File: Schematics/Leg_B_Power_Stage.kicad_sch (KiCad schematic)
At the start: 38 parts, among them Q4 C3M0025065K, Q5 C3M0025065K, U3 UCC21710QDWRQ1, U4 UCC21710QDWRQ1

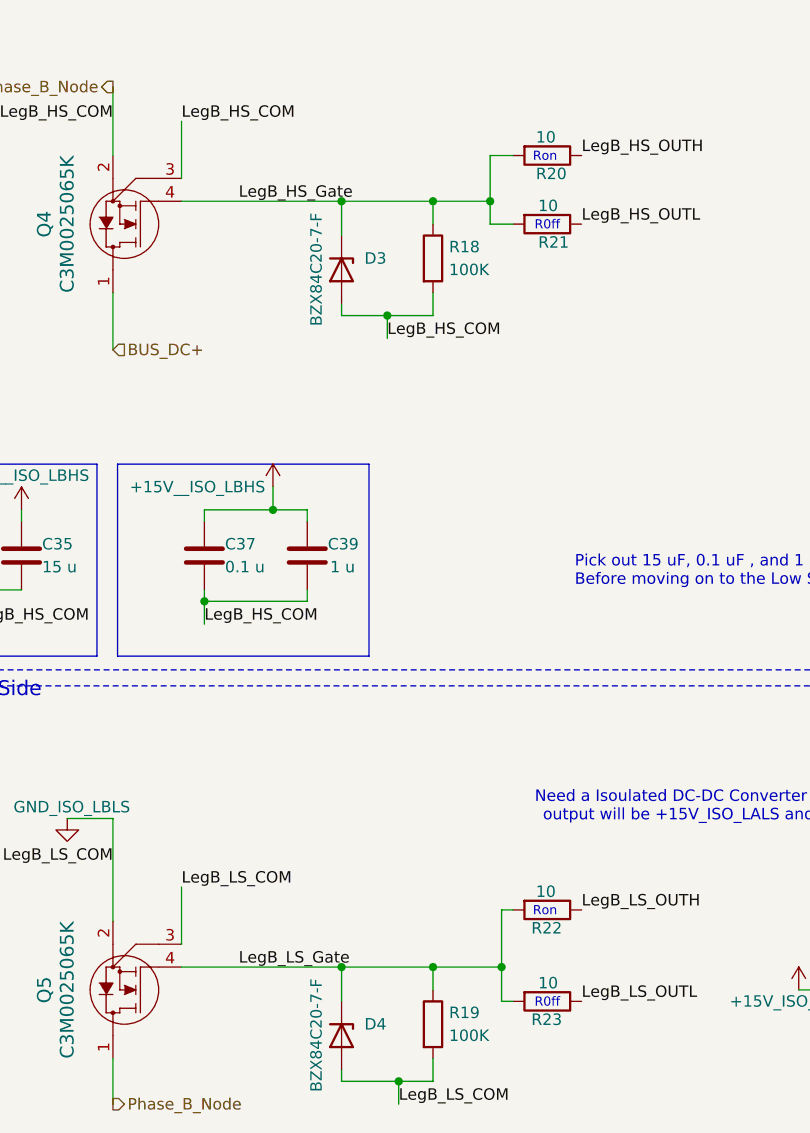
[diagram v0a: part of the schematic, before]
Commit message: [Milestone Compelted Controller and USB]
- Added Test Points
- Completed USB circuit to Controller
- Wired up Controller
- Added Connectors to Power Subsheet and 12pin from cotnroller to Full
  Bridge
- Added 3d models for USB compoents
- General fixes to subsheets
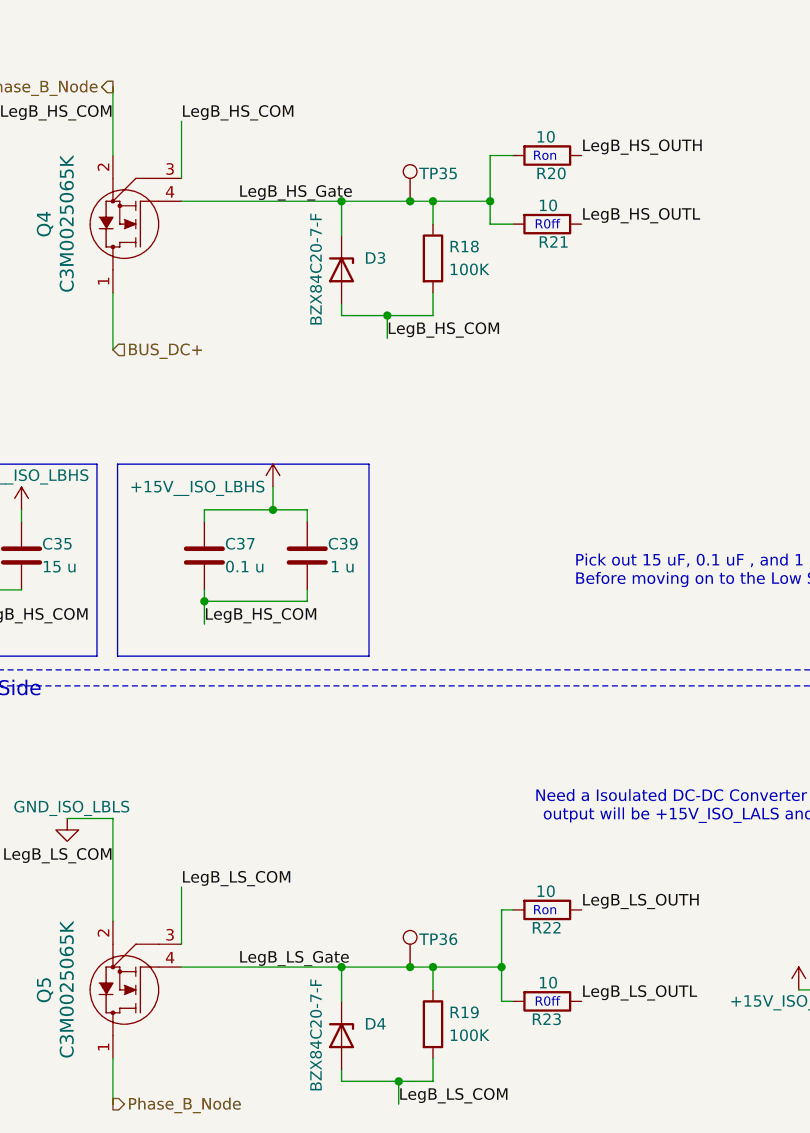
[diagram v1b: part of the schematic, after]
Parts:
- added TP35, TP36: 5277, SiC_Inverter:5277, symbol SiC_Inverter:5277
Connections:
- net LegB_HS_Gate: now also TP35.1
- net LegB_LS_Gate: now also TP36.1
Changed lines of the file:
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@@
 	)
 	(junction
+		(at 67.31 54.61)
+		(diameter 0)
+		(color 0 0 0 0)
+	)
+	(junction
 		(at 181.61 69.85)
 		(diameter 0)
@@
 	)
 	(junction
+		(at 67.31 139.7)
+		(diameter 0)
+		(color 0 0 0 0)
+	)
+	(junction
 		(at 207.01 53.34)
 		(diameter 0)
@@
 	(wire
 		(pts
-			(xy 59.69 54.61) (xy 69.85 54.61)
+			(xy 59.69 54.61) (xy 67.31 54.61)
 		)
 		(stroke
@@
 	(wire
 		(pts
-			(xy 59.69 139.7) (xy 69.85 139.7)
+			(xy 59.69 139.7) (xy 67.31 139.7)
 		)
 		(stroke
@@
 	(wire
 		(pts
+			(xy 67.31 54.61) (xy 69.85 54.61)
+		)
+		(stroke
+			(width 0)
+			(type default)
+		)
+	)
+	(wire
+		(pts
 			(xy 69.85 139.7) (xy 69.85 142.24)
 		)
@@
 	(wire
 		(pts
+			(xy 67.31 139.7) (xy 69.85 139.7)
+		)
+		(stroke
+			(width 0)
+			(type default)
+		)
+	)
+	(wire
+		(pts
 			(xy 44.45 88.9) (xy 44.45 90.17)
 		)
@@
 	)
 	(symbol
+		(lib_id "SiC_Inverter:5277")
+		(at 67.31 139.7 0)
+		(unit 1)
+		(exclude_from_sim no)
+		(in_bom yes)
+		(on_board yes)
+		(dnp no)
+		(property "Reference" "TP36"
+			(at 68.326 136.652 0)
+			(effects
+				(font
+					(size 1.27 1.27)
+				)
+				(justify left)
+			)
+		)
+		(property "Value" "5277"
+			(at 51.308 152.654 0)
+			(effects
+				(font
+					(size 1.27 1.27)
+				)
+				(hide yes)
+			)
+		)
+		(property "Footprint" "SiC_Inverter:5277"
+			(at 57.404 150.876 0)
+			(effects
+				(font
+					(size 1.27 1.27)
+				)
+				(hide yes)
+			)
+		)
+		(property "Datasheet" "https://www.keyelco.com/userAssets/file/K75p62.pdf"
+			(at 75.184 147.066 0)
+			(effects
+				(font
+					(size 1.27 1.27)
+				)
+				(hide yes)
+			)
+		)
+		(property "Description" "Test Plugs & Test Jacks TEST POINT (BLUE) - COMPACT"
+			(at 77.724 149.098 0)
+			(effects
+				(font
+					(size 1.27 1.27)
+				)
+				(hide yes)
+			)
+		)
+		(pin "1"
+		)
+		(instances
+			(project "SiC_Single_Phase_Inverter"
+				(path "/a1ed0539-9735-4ad1-a8fd-87e26e7fce16/b6e78e1f-718a-4f31-892b-d9c389541b0d/d1761b4e-8a42-4386-8dfd-35f782fbcef3"
+					(reference "TP36")
+					(unit 1)
+				)
+			)
+		)
+	)
+	(symbol
 		(lib_id "SiC_Inverter:C3216X5R1E156M160AB")
 		(at 24.13 93.98 0)
@@
 					(unit 1)
 				)
+			)
+		)
+	)
+	(symbol
+		(lib_id "SiC_Inverter:5277")
+		(at 67.31 54.61 0)
+		(unit 1)
+		(exclude_from_sim no)
+		(in_bom yes)
+		(on_board yes)
+		(dnp no)
+		(property "Reference" "TP35"
+			(at 68.326 51.562 0)
+			(effects
+				(font
+					(size 1.27 1.27)
+				)
+				(justify left)
+			)
+		)
+		(property "Value" "5277"
+			(at 51.308 67.564 0)
+			(effects
+				(font
+					(size 1.27 1.27)
+				)
+				(hide yes)
+			)
+		)
+		(property "Footprint" "SiC_Inverter:5277"
+			(at 57.404 65.786 0)
+			(effects
+				(font
+					(size 1.27 1.27)
+				)
+				(hide yes)
+			)
+		)
+		(property "Datasheet" "https://www.keyelco.com/userAssets/file/K75p62.pdf"
+			(at 75.184 61.976 0)
+			(effects
+				(font
+					(size 1.27 1.27)
+				)
+				(hide yes)
+			)
+		)
+		(property "Description" "Test Plugs & Test Jacks TEST POINT (BLUE) - COMPACT"
+			(at 77.724 64.008 0)
+			(effects
+				(font
+					(size 1.27 1.27)
+				)
+				(hide yes)
+			)
+		)
+		(pin "1"
+		)
+		(instances
+			(project "SiC_Single_Phase_Inverter"
+				(path "/a1ed0539-9735-4ad1-a8fd-87e26e7fce16/b6e78e1f-718a-4f31-892b-d9c389541b0d/d1761b4e-8a42-4386-8dfd-35f782fbcef3"
+					(reference "TP35")
+					(unit 1)
+				)

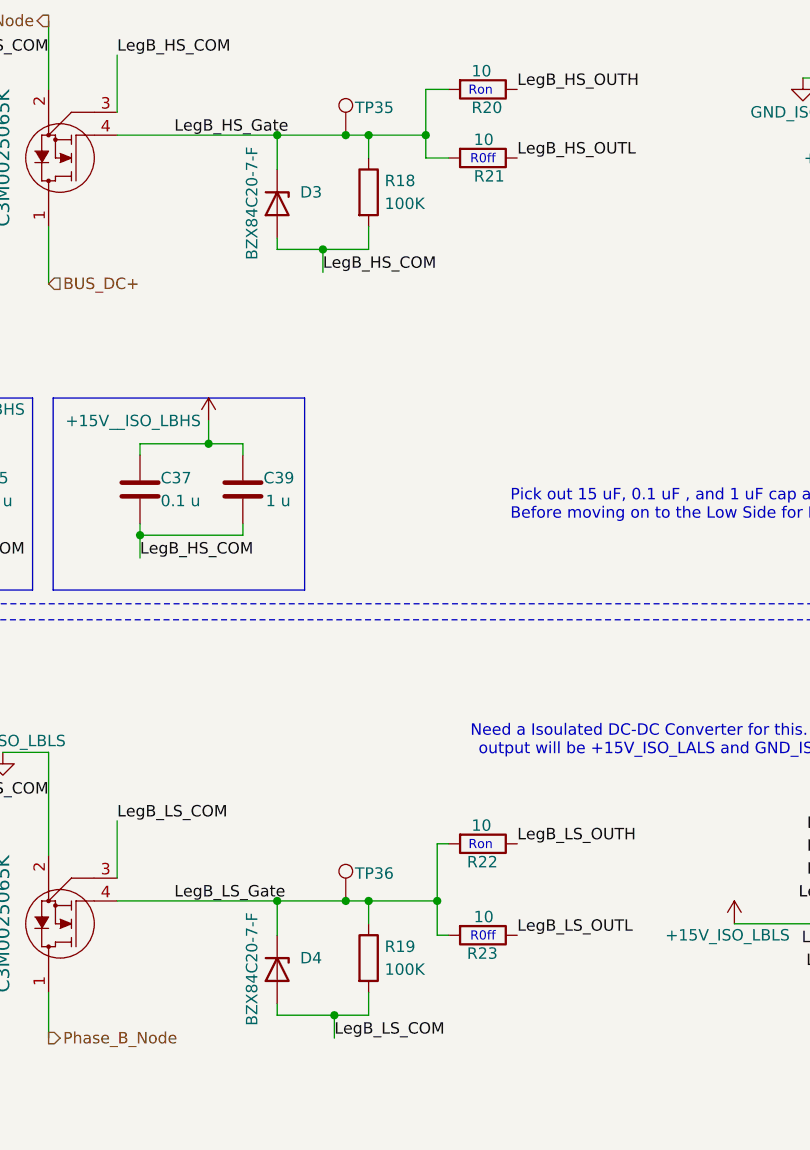
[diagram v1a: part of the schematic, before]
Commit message: [WIP Input Protection Circuit to Controller]
- Added Gate node input protection pin to controller
- Added optocoupler to input protection circuit
- Added 3d model for PC817.....
- Updated PCB to test out PCB modularity
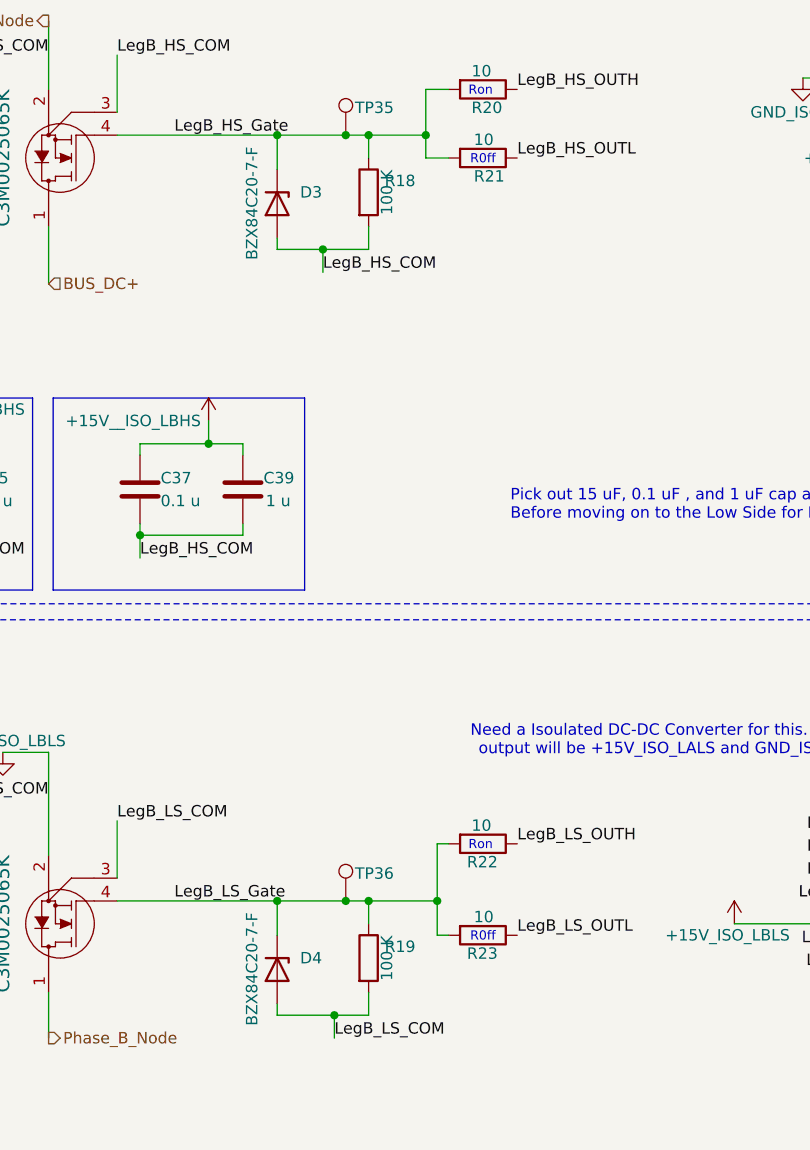
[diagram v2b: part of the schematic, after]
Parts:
- R18, R19: value 100K -> 100 K; symbol Device:R -> SiC_Inverter:RT1206BRD07100KL
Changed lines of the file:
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@@
 	)
 	(symbol
-		(lib_id "Device:R")
+		(lib_id "SiC_Inverter:RT1206BRD07100KL")
 		(at 69.85 60.96 0)
 		(unit 1)
@@
 			)
 		)
-		(property "Value" "100K"
-			(at 71.628 62.23 0)
-			(effects
-				(font
-					(size 1.27 1.27)
-				)
-				(justify left)
+		(property "Value" "100 K"
+			(at 71.882 60.96 90)
+			(effects
+				(font
+					(size 1.27 1.27)
+				)
 			)
 		)
 		(property "Footprint" "Resistor_SMD:R_1206_3216Metric_Pad1.30x1.75mm_HandSolder"
-			(at 68.072 60.96 90)
-			(effects
-				(font
-					(size 1.27 1.27)
-				)
-				(hide yes)
-			)
-		)
-		(property "Datasheet" "~"
-			(at 69.85 60.96 0)
-			(effects
-				(font
-					(size 1.27 1.27)
-				)
-				(hide yes)
-			)
-		)
-		(property "Description" "Resistor"
-			(at 69.85 60.96 0)
+			(at 82.804 72.39 0)
+			(effects
+				(font
+					(size 1.27 1.27)
+				)
+				(hide yes)
+			)
+		)
+		(property "Datasheet" "https://www.mouser.com/datasheet/3/508/1/PYu-RT_1-to-0.01_RoHS_L_15.pdf"
+			(at 92.202 74.676 0)
+			(effects
+				(font
+					(size 1.27 1.27)
+				)
+				(hide yes)
+			)
+		)
+		(property "Description" "Thin Film Resistors - SMD 1/4W 5K ohm .1% 25ppm"
+			(at 78.486 76.962 0)
 			(effects
 				(font
@@
 	)
 	(symbol
-		(lib_id "Device:R")
+		(lib_id "SiC_Inverter:RT1206BRD07100KL")
 		(at 69.85 146.05 0)
 		(unit 1)
@@
 			)
 		)
-		(property "Value" "100K"
-			(at 71.628 147.32 0)
-			(effects
-				(font
-					(size 1.27 1.27)
-				)
-				(justify left)
+		(property "Value" "100 K"
+			(at 71.882 146.05 90)
+			(effects
+				(font
+					(size 1.27 1.27)
+				)
 			)
 		)
 		(property "Footprint" "Resistor_SMD:R_1206_3216Metric_Pad1.30x1.75mm_HandSolder"
-			(at 68.072 146.05 90)
-			(effects
-				(font
-					(size 1.27 1.27)
-				)
-				(hide yes)
-			)
-		)
-		(property "Datasheet" "~"
-			(at 69.85 146.05 0)
-			(effects
-				(font
-					(size 1.27 1.27)
-				)
-				(hide yes)
-			)
-		)
-		(property "Description" "Resistor"
-			(at 69.85 146.05 0)
-			(effects
-				(font
+			(at 82.804 157.48 0)
+			(effects
+				(font
+					(size 1.27 1.27)
+				)
+				(hide yes)
+			)
+		)
+		(property "Datasheet" "https://www.mouser.com/datasheet/3/508/1/PYu-RT_1-to-0.01_RoHS_L_15.pdf"
+			(at 92.202 159.766 0)
+			(effects
+				(font
+					(size 1.27 1.27)
+				)
+				(hide yes)
+			)
+		)
+		(property "Description" "Thin Film Resistors - SMD 1/4W 5K ohm .1% 25ppm"
+			(at 78.486 162.052 0)
+			(effects
+				(font

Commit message: WIP PCB, Added Test Points, added icon file
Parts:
- renumbered D3 to D4, D4 to D5, R18 to R19, R19 to R20, R20 to R21, R21 to R22, R22 to R23, R23 to R24, R24 to R25, R25 to R26, R26 to R27, R27 to R28, R28 to R29, R29 to R30, R30 to R31, R31 to R32, TP35 to TP36, TP36 to TP37
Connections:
- net LegB_HS_Gate: no longer TP36.1
- net LegB_LS_Gate: no longer TP37.1
